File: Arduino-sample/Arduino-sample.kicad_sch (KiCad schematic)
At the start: 21 parts, among them J1 Conn_01x06_Pin, J2 Conn_01x12_Pin, J3 Conn_01x12_Pin, SW1 SW_Push, U1 NJM78L05SU3, U2 ATmega328P-A, Y1 CSTCE16M0V53-R0

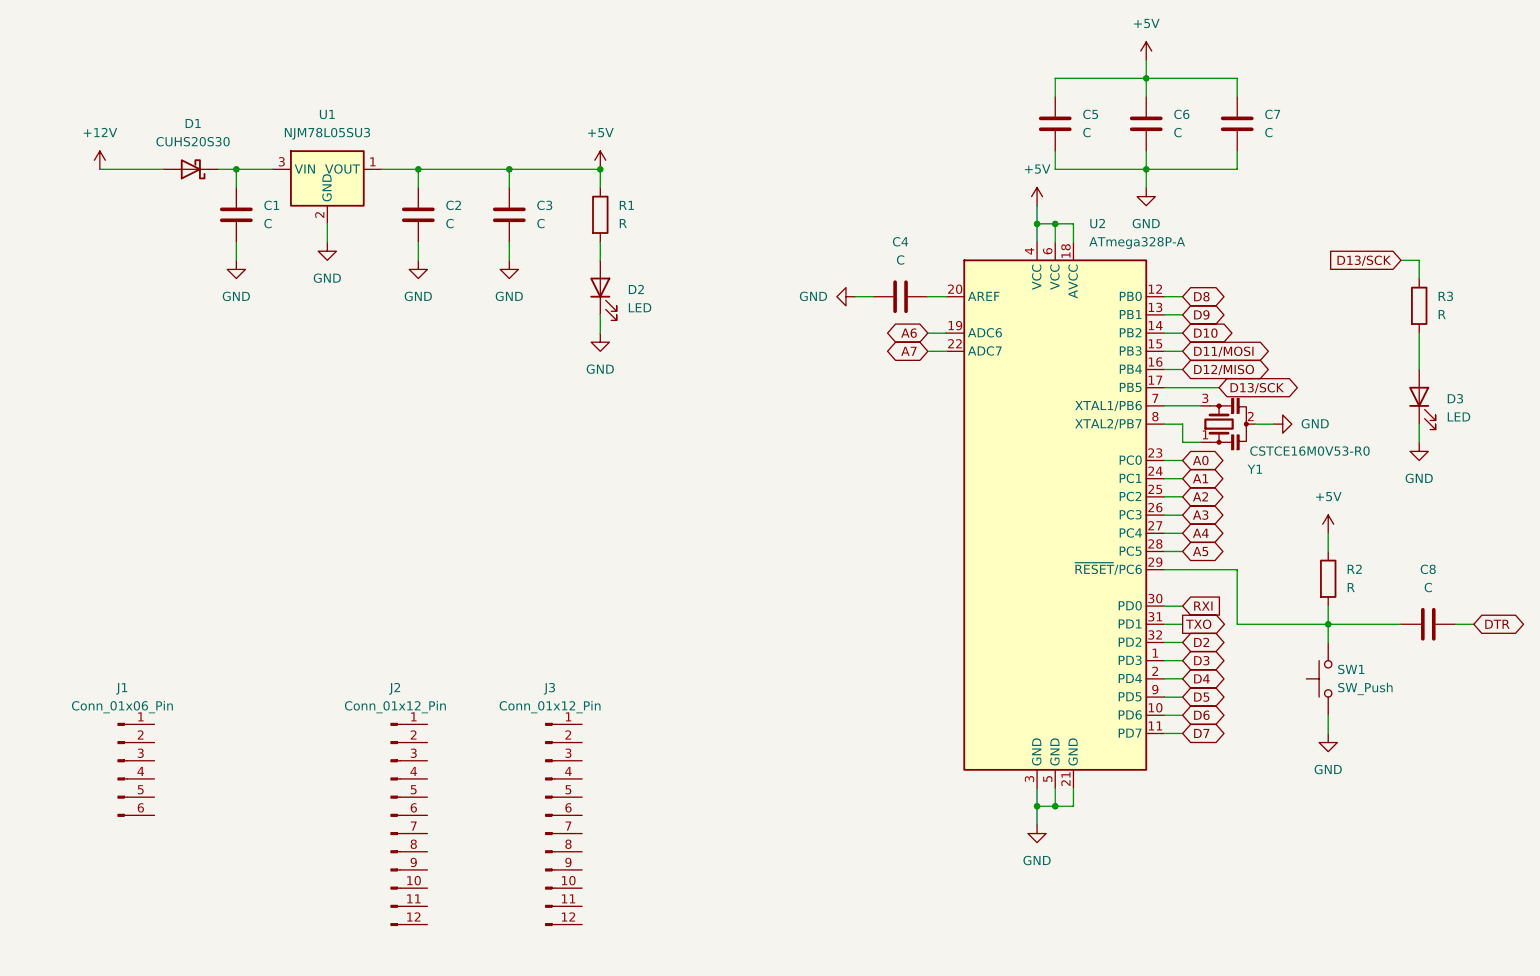
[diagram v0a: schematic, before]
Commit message: ピンヘッダ配線追加
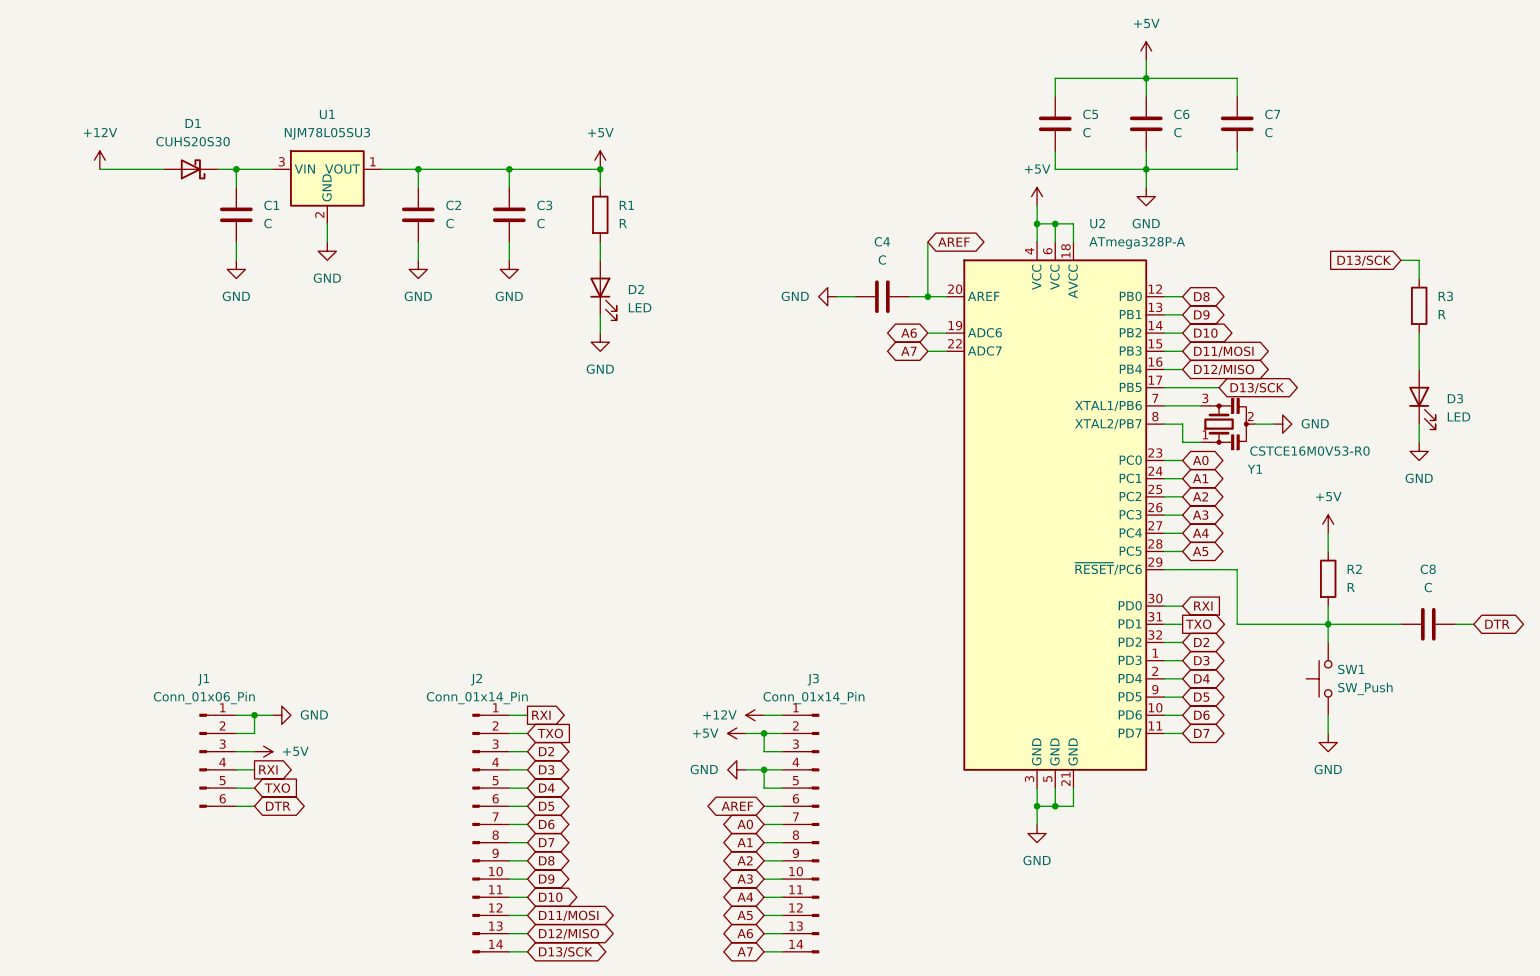
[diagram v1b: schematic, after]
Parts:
- removed J2, J3: Conn_01x12_Pin, symbol Connector:Conn_01x12_Pin
- added J2, J3: Conn_01x14_Pin, symbol Connector:Conn_01x14_Pin
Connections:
- net +12V: now also J3.1 (Pin_1)
- net +5V: now also J1.3 (Pin_3), J3.2 (Pin_2), J3.3 (Pin_3)
- net A0: now also J3.7 (Pin_7)
- net A1: now also J3.8 (Pin_8)
- net A2: now also J3.9 (Pin_9)
- net A3: now also J3.10 (Pin_10)
- net A4: now also J3.11 (Pin_11)
- net A5: now also J3.12 (Pin_12)
- net A6: now also J3.13 (Pin_13)
- net A7: now also J3.14 (Pin_14)
- net D10: now also J2.11 (Pin_11)
- net D11/MOSI: now also J2.12 (Pin_12)
- net D12/MISO: now also J2.13 (Pin_13)
- net D13/SCK: now also J2.14 (Pin_14)
- net D2: now also J2.3 (Pin_3)
- net D3: now also J2.4 (Pin_4)
- net D4: now also J2.5 (Pin_5)
- net D5: now also J2.6 (Pin_6)
- net D6: now also J2.7 (Pin_7)
- net D7: now also J2.8 (Pin_8)
- net D8: now also J2.9 (Pin_9)
- net D9: now also J2.10 (Pin_10)
- net DTR: now also J1.6 (Pin_6)
- net GND: now also J1.1 (Pin_1), J1.2 (Pin_2), J3.4 (Pin_4), J3.5 (Pin_5)
- net RXI: now also J1.4 (Pin_4), J2.1 (Pin_1)
- net TXO: now also J1.5 (Pin_5), J2.2 (Pin_2)
- net AREF: now reaches C4.2, U2.20 (AREF)
- net AREF: now also J3.6 (Pin_6)
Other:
- moved on the sheet: C4, J1

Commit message: シンボル修正版に置き換え、pwr_flag追加
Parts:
- removed D1: CUHS20S30, ProjectEV:CUHS20S30, symbol ProjectEV:CUHS20S30
- removed U1: NJM78L05SU3, ProjectEV:SOT-89-3, symbol ProjectEV:NJM78L05SU3
- removed U2: ATmega328P-A, ProjectEV:TQFP-32_7x7mm_P0.8mm, symbol ProjectEV:ATmega328P-A
- removed Y1: CSTCE16M0V53-R0, ProjectEV:CSTCE16M0V53-R0, symbol ProjectEV:CSTCE16M0V53-R0
- added D1: CUHS20S30, ProjectEV:CUHS20S30, symbol ProjectEV:D_CUHS20S30
- added U1: NJM78L05SU3, ProjectEV:SOT-89-3, symbol ProjectEV:Regulator_NJM78L05SU3
- added U2: ATmega328P-A, ProjectEV:TQFP-32_7x7mm_P0.8mm, symbol ProjectEV:MCU_ATmega328P-A
- added Y1: CSTCE16M0V53-R0, ProjectEV:CSTCE16M0V53-R0, symbol ProjectEV:Resonator_CSTCE16M0V53-R0
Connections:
- net +12V: now also D1.2 (A)
- net +5V: now also U1.1 (VOUT), U2.18 (AVCC), U2.4 (VCC), U2.6 (VCC)
- net A0: now also U2.23 (PC0)
- net A1: now also U2.24 (PC1)
- net A2: now also U2.25 (PC2)
- net A3: now also U2.26 (PC3)
- net A4: now also U2.27 (PC4)
- net A5: now also U2.28 (PC5)
- net A6: now also U2.19 (ADC6)
- net A7: now also U2.22 (ADC7)
- net AREF: now also U2.20 (AREF)
- net D10: now also U2.14 (PB2)
- net D11/MOSI: now also U2.15 (PB3)
- net D12/MISO: now also U2.16 (PB4)
- net D13/SCK: now also U2.17 (PB5)
- net D2: now also U2.32 (PD2)
- net D3: now also U2.1 (PD3)
- net D4: now also U2.2 (PD4)
- net D5: now also U2.9 (PD5)
- net D6: now also U2.10 (PD6)
- net D7: now also U2.11 (PD7)
- net D8: now also U2.12 (PB0)
- net D9: now also U2.13 (PB1)
- net GND: now also U1.2 (GND), U2.21 (GND), U2.3 (GND), U2.5 (GND), Y1.2
- net RXI: now also U2.30 (PD0)
- net TXO: now also U2.31 (PD1)
- net at C8.1, R2.2, SW1.2: now also U2.29 (~{RESET}/PC6)
- net at C1.1: now also D1.1 (K), U1.3 (VIN)
- new net: U2.8 (XTAL2/PB7), Y1.1
- new net: U2.7 (XTAL1/PB6), Y1.3

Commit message: update symbol from library
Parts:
- D1: footprint ProjectEV:CUHS20S30 -> ProjectEV:D_CUHS20S30
- U1: footprint ProjectEV:SOT-89-3 -> ProjectEV:Package_SOT-89-3
- U2: footprint ProjectEV:TQFP-32_7x7mm_P0.8mm -> ProjectEV:Package_TQFP-32_7x7mm_P0.8mm
- Y1: footprint ProjectEV:CSTCE16M0V53-R0 -> ProjectEV:Resonator_CSTCE16M0V53-R0
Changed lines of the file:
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@@
       (effects (font (size 1.27 1.27)))
     )
-    (property "Footprint" "ProjectEV:CUHS20S30" (at 57.15 50.8 0)
+    (property "Footprint" "ProjectEV:D_CUHS20S30" (at 57.15 50.8 0)
       (effects (font (size 1.27 1.27)) hide)
     )
@@
       (effects (font (size 1.27 1.27)))
     )
-    (property "Footprint" "ProjectEV:CSTCE16M0V53-R0" (at 200.66 86.995 0)
+    (property "Footprint" "ProjectEV:Resonator_CSTCE16M0V53-R0" (at 200.66 86.995 0)
       (effects (font (size 1.27 1.27)) hide)
     )
@@
       (effects (font (size 1.27 1.27)))
     )
-    (property "Footprint" "ProjectEV:SOT-89-3" (at 76.2 45.085 0)
+    (property "Footprint" "ProjectEV:Package_SOT-89-3" (at 76.2 45.085 0)
       (effects (font (size 1.27 1.27) italic) hide)
     )
@@
       (effects (font (size 1.27 1.27)) (justify left))
     )
-    (property "Footprint" "ProjectEV:TQFP-32_7x7mm_P0.8mm" (at 177.8 99.06 0)
+    (property "Footprint" "ProjectEV:Package_TQFP-32_7x7mm_P0.8mm" (at 177.8 99.06 0)
       (effects (font (size 1.27 1.27) italic) hide)
     )
